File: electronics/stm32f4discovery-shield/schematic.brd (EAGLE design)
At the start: 101.6 x 105.4 mm, 43 parts, among them IC1 MAX3468CPA, IC3 LM340H-12, IC4 LM340H-12, J1 POWER_JACKSLT, Q1 BC548

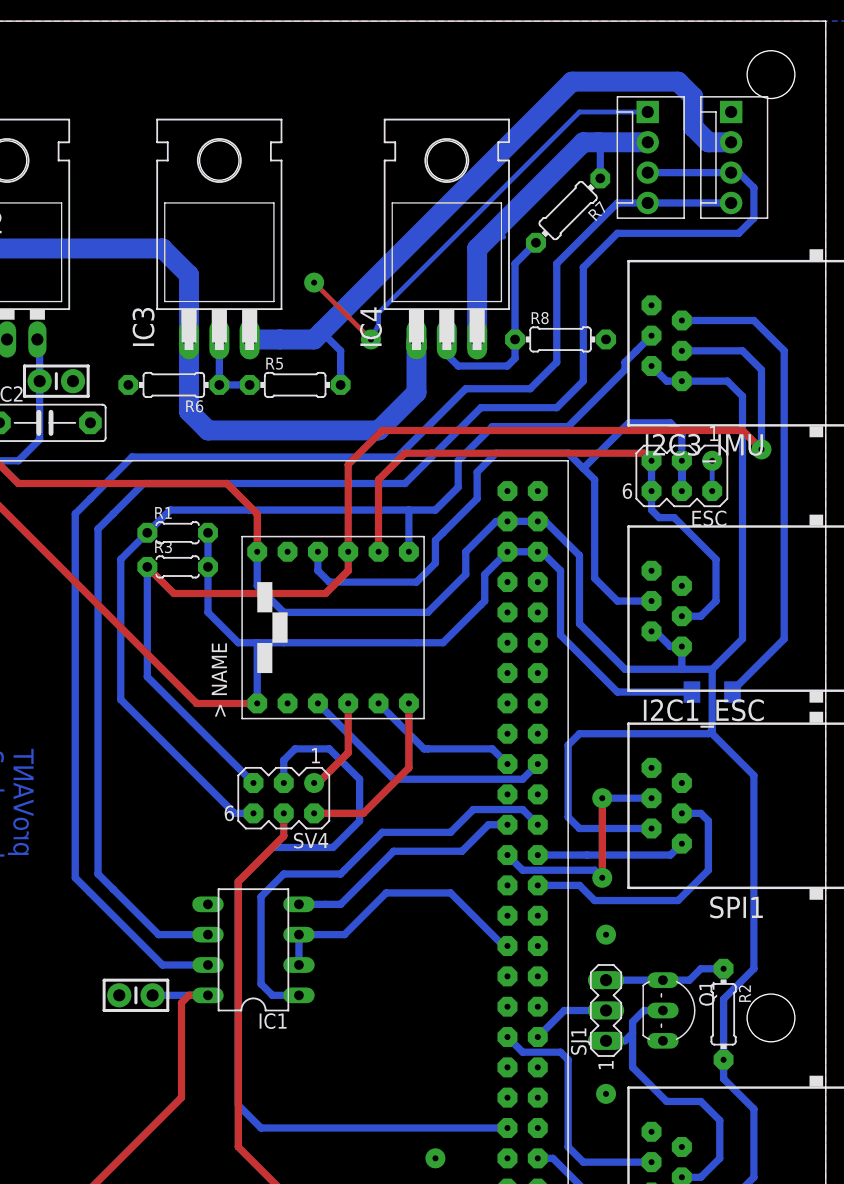
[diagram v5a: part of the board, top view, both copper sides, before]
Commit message: Mounting holes na placa.
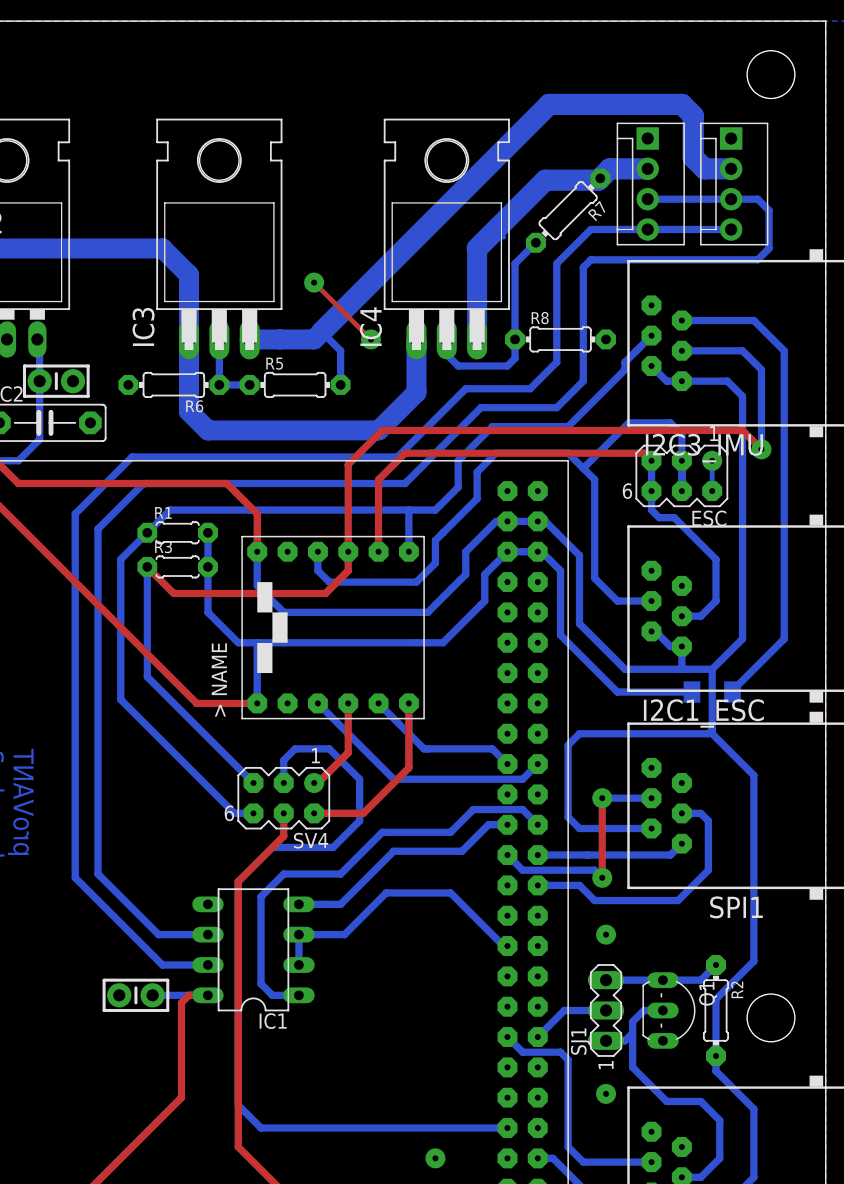
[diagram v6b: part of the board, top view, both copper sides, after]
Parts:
- moved SRVO1 2.22 mm to (86.7, 100.6)
- moved SRVO2 2.22 mm to (93.7, 100.6)
- moved R2 0.71 mm to (92.4, 27.6)
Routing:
- net GND: track 41.2 -> 9.28 mm
- net SRVO1_PWR: track 38.4 -> 34.3 mm
- net D+/TX: track 123.5 -> 125.4 mm
- net D-/RX: track 115.2 -> 114.2 mm
- net 5V: track 398.8 -> 399.3 mm
- net N$3: track 10.2 -> 9.73 mm

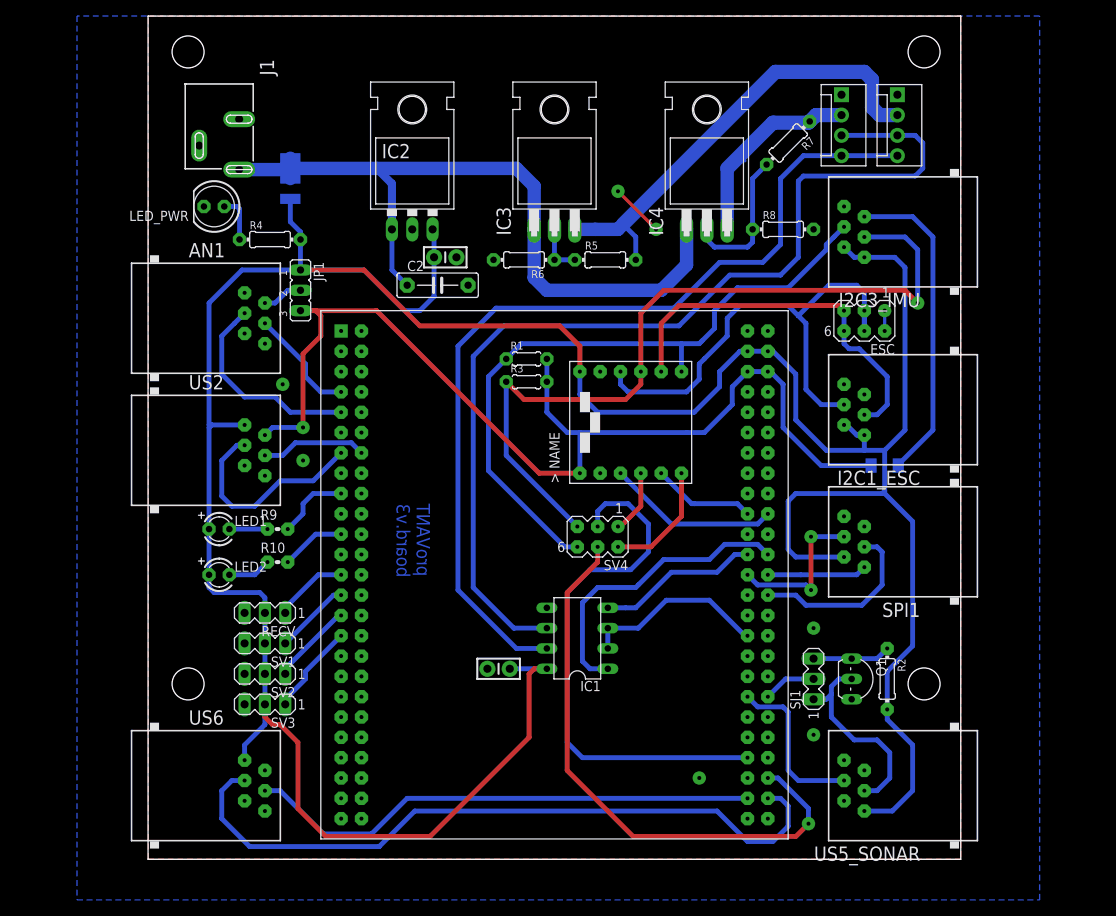
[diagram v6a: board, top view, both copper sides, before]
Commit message: Correcoes finais a placa.
- Conectores RECV, SV1, SV2 e SV3 movidos mais para a borda da placa.
- 5V disponiveis no pino 2 do conector US6.
- Conector US5_SONAR renomeado para US3_SONAR (por usar a USART3)
- No conector I2C3_IMU, GND disponivel agora no pino 2 e 3v3 no pino 1.
- Pino de GND do MAX485 ok (antes desconectado da malha de terra).
- GND disponivel nos pinos 5 e 6 do conector US3_SONAR.

	modified:   electronics/stm32f4discovery-shield/schematic.brd
	modified:   electronics/stm32f4discovery-shield/schematic.sch
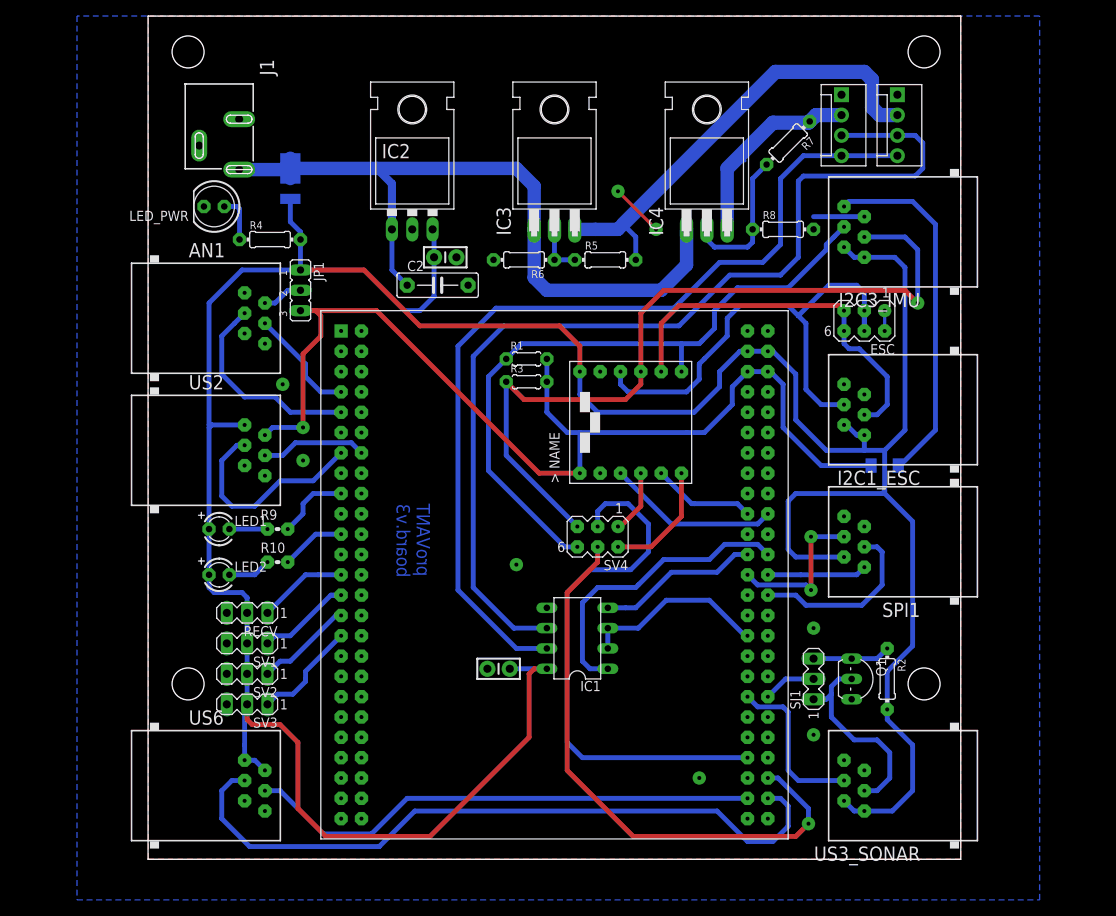
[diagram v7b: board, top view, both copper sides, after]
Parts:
- moved RECV 2.22 mm to (12.4, 35.9)
- moved SV1 2.22 mm to (12.4, 32.1)
- moved SV2 2.22 mm to (12.4, 28.3)
- moved SV3 2.22 mm to (12.4, 24.4)
- renumbered US5_SONAR to US3_SONAR
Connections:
- net 5V: now also US3_SONAR.1, US6.1
- net GND: now also I2C3_IMU.6; no longer I2C3_IMU.5
- net N$10: now also AN1.2
- net N$9: now also I2C3_IMU.5; no longer I2C3_IMU.6
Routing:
- net GND: track 9.28 -> 15.6 mm
- net 5V: track 399.3 -> 404.7 mm
- net N$9: track 40.0 -> 45.1 mm
- net PE9/PWM: track 9.48 -> 11.7 mm
- net PE13/PWM: track 11.5 -> 13.5 mm
- net PE11/PWM: track 10.4 -> 12.2 mm
- net PE7: track 9.33 -> 11.2 mm
